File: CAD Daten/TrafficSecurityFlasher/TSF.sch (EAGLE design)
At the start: 5 parts, among them IC1 TINY15LS

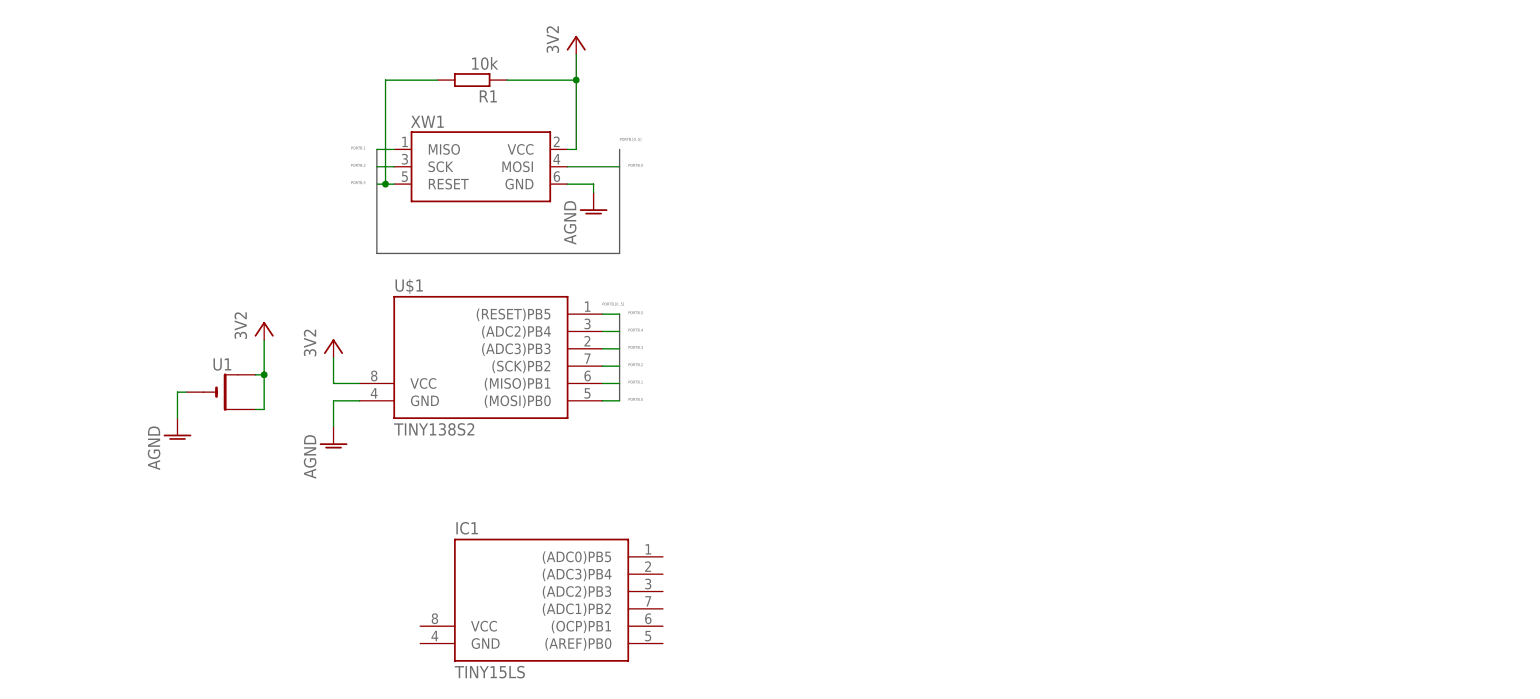
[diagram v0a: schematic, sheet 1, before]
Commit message: 
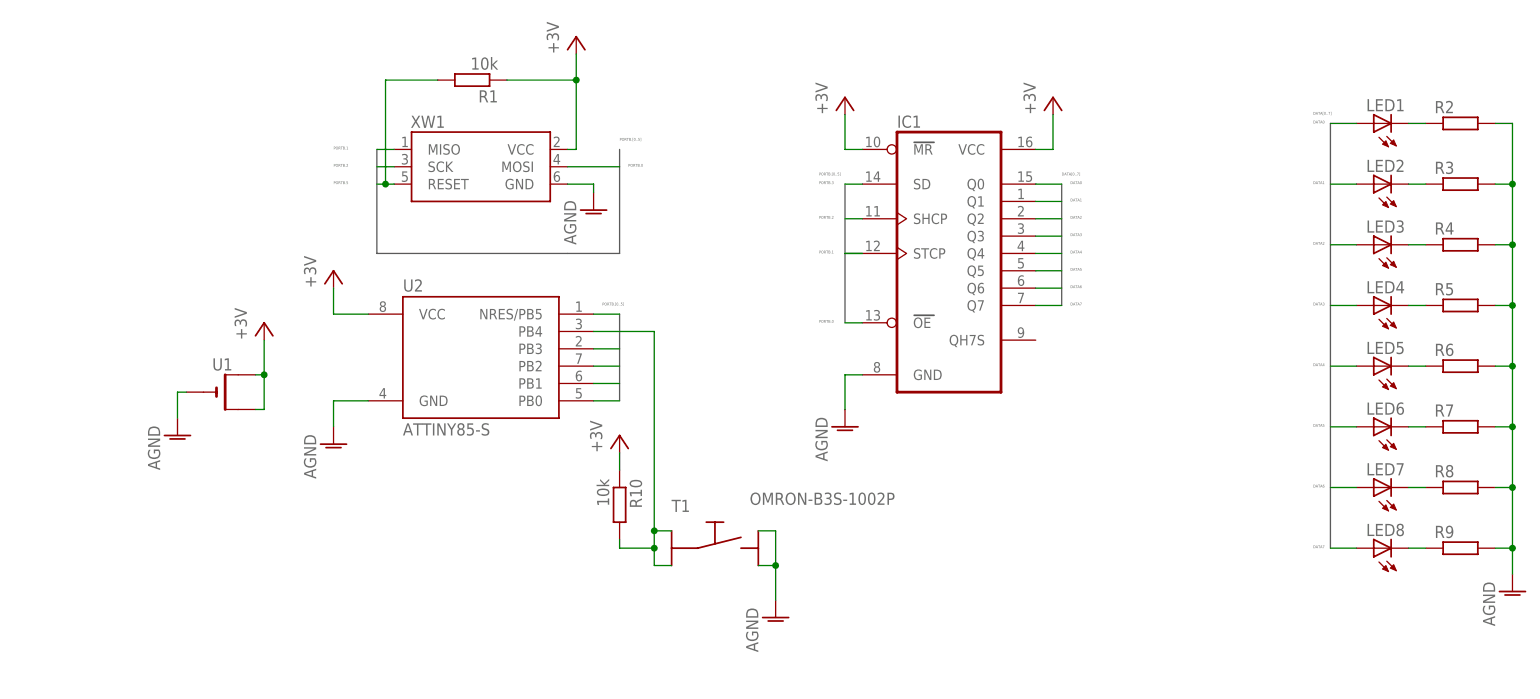
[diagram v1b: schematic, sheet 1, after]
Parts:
- removed U$1: TINY138S2, Atmel - µController:TINY138S2
- added LED1, LED2, LED3, LED4, LED5, LED6, LED7, LED8: (no value), led:LEDP-LCC-2
- added R10: 10k, rcl:R-EU_R1206
- added R2, R3, R4, R5, R6, R7, R8, R9: (no value), rcl:R-EU_M1206
- added T1: OMRON-B3S-1002P, Taster - Omron B3S-1002P:OMRON-B3S-1002P
- added U2: ATTINY85-S, _hhn_attiny25_45_85:ATTINY85-S
- IC1: value TINY15LS -> (none); device atmel:TINY15LS -> 74_er Reihe (DIN Europa):74HC595D
- XW1: device Atmel - ISP_6 (AVR ISP MKII):WSL6 -> Atmel - ISP_6 (AVR ISP MKII):WSLSMD
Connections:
- removed net +3V2: R1.1, U$1.VCC, U1.+, U1.+1, XW1.VCC
- new net DATA0: IC1.Q0, LED1.A
- new net DATA1: IC1.Q1, LED2.A
- new net DATA2: IC1.Q2, LED3.A
- new net DATA3: IC1.Q3, LED4.A
- new net DATA4: IC1.Q4, LED5.A
- new net DATA5: IC1.Q5, LED6.A
- new net DATA6: IC1.Q6, LED7.A
- new net DATA7: IC1.Q7, LED8.A
- new net GND: XW1.GND
- new net N$10: LED5.C, R6.1
- new net N$11: LED6.C, R7.1
- new net N$12: LED7.C, R8.1
- new net N$13: LED8.C, R9.1
- new net N$6: LED1.C, R2.1
- new net N$7: LED2.C, R3.1
- new net N$8: LED3.C, R4.1
- new net N$9: LED4.C, R5.1
- new net VCC: IC1.MR, IC1.VCC, R1.1, R10.1, U1.+, U1.+1, XW1.VCC
- net AGND: now also IC1.GND, R2.2, R3.2, R4.2, R5.2, R6.2, R7.2, R8.2, R9.2, T1.3, T1.4; no longer U$1.GND, XW1.GND
- net PORTB.0: now also IC1.OE, U2.PB0; no longer U$1.(MOSI)PB0
- net PORTB.1: now also IC1.STCP, U2.PB1; no longer U$1.(MISO)PB1
- net PORTB.2: now also IC1.SHCP, U2.PB2; no longer U$1.(SCK)PB2
- net PORTB.3: now also IC1.SD, U2.PB3; no longer U$1.(ADC3)PB3
- net PORTB.4: now also R10.2, T1.1, T1.2, U2.PB4; no longer U$1.(ADC2)PB4
- net PORTB.5: now also U2.NRES/PB5; no longer U$1.(RESET)PB5

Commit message: 
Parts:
- added PAD1, PAD2: (no value), wirepad:SMD2
- added SJ1: (no value), jumper:SJW
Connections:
- new net N$1: SJ1.1, U1.+, U1.+1
- net AGND: now also PAD2.P
- net VCC: now also PAD1.P, SJ1.2; no longer U1.+, U1.+1
